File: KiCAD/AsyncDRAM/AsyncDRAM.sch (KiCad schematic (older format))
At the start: 6 parts

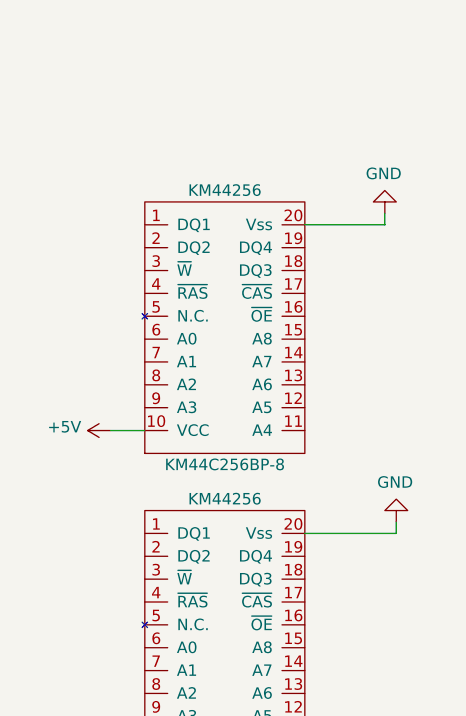
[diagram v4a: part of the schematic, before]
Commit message: Added ATmega809 Symbol
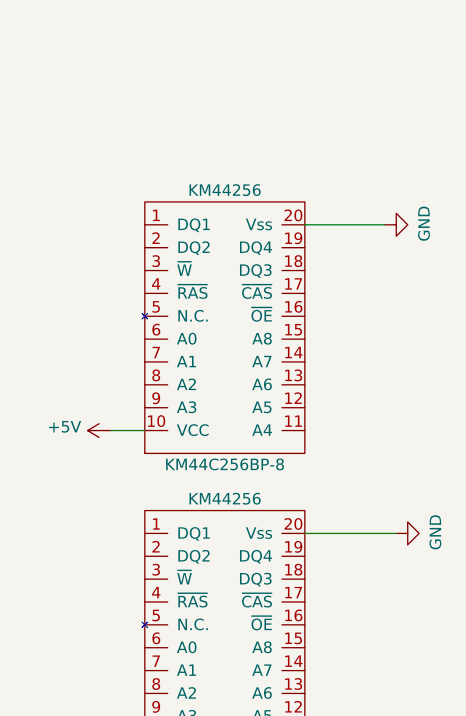
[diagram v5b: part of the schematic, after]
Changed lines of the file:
@@
 L Power:GND #PWR?
 U 1 1 5DAAFE76
-P 5300 1500
-F 0 "#PWR?" H 5300 1250 50  0001 C CNN
-F 1 "GND" H 5305 1327 50  0000 C CNN
-F 2 "" H 5300 1500 50  0001 C CNN
-F 3 "" H 5300 1500 50  0001 C CNN
-	1    5300 1500
-	-1   0    0    1
+P 5300 1550
+F 0 "#PWR?" H 5300 1300 50  0001 C CNN
+F 1 "GND" H 5305 1377 50  0000 C CNN
+F 2 "" H 5300 1550 50  0001 C CNN
+F 3 "" H 5300 1550 50  0001 C CNN
+	1    5300 1550
+	0    -1   -1   0
 $EndComp
 Wire Wire Line
 	4950 1550 5300 1550
-Wire Wire Line
-	5300 1550 5300 1500
 $Comp
 L Power:+5V #PWR?
@@
 L Power:GND #PWR?
 U 1 1 5DAB36DC
-P 5350 2850
-F 0 "#PWR?" H 5350 2600 50  0001 C CNN
-F 1 "GND" H 5355 2677 50  0000 C CNN
-F 2 "" H 5350 2850 50  0001 C CNN
-F 3 "" H 5350 2850 50  0001 C CNN
-	1    5350 2850
-	-1   0    0    1
+P 5350 2900
+F 0 "#PWR?" H 5350 2650 50  0001 C CNN
+F 1 "GND" H 5355 2727 50  0000 C CNN
+F 2 "" H 5350 2900 50  0001 C CNN
+F 3 "" H 5350 2900 50  0001 C CNN
+	1    5350 2900
+	0    -1   -1   0
 $EndComp
 Wire Wire Line
 	4950 2900 5350 2900
-Wire Wire Line
-	5350 2900 5350 2850
 $EndSCHEMATC

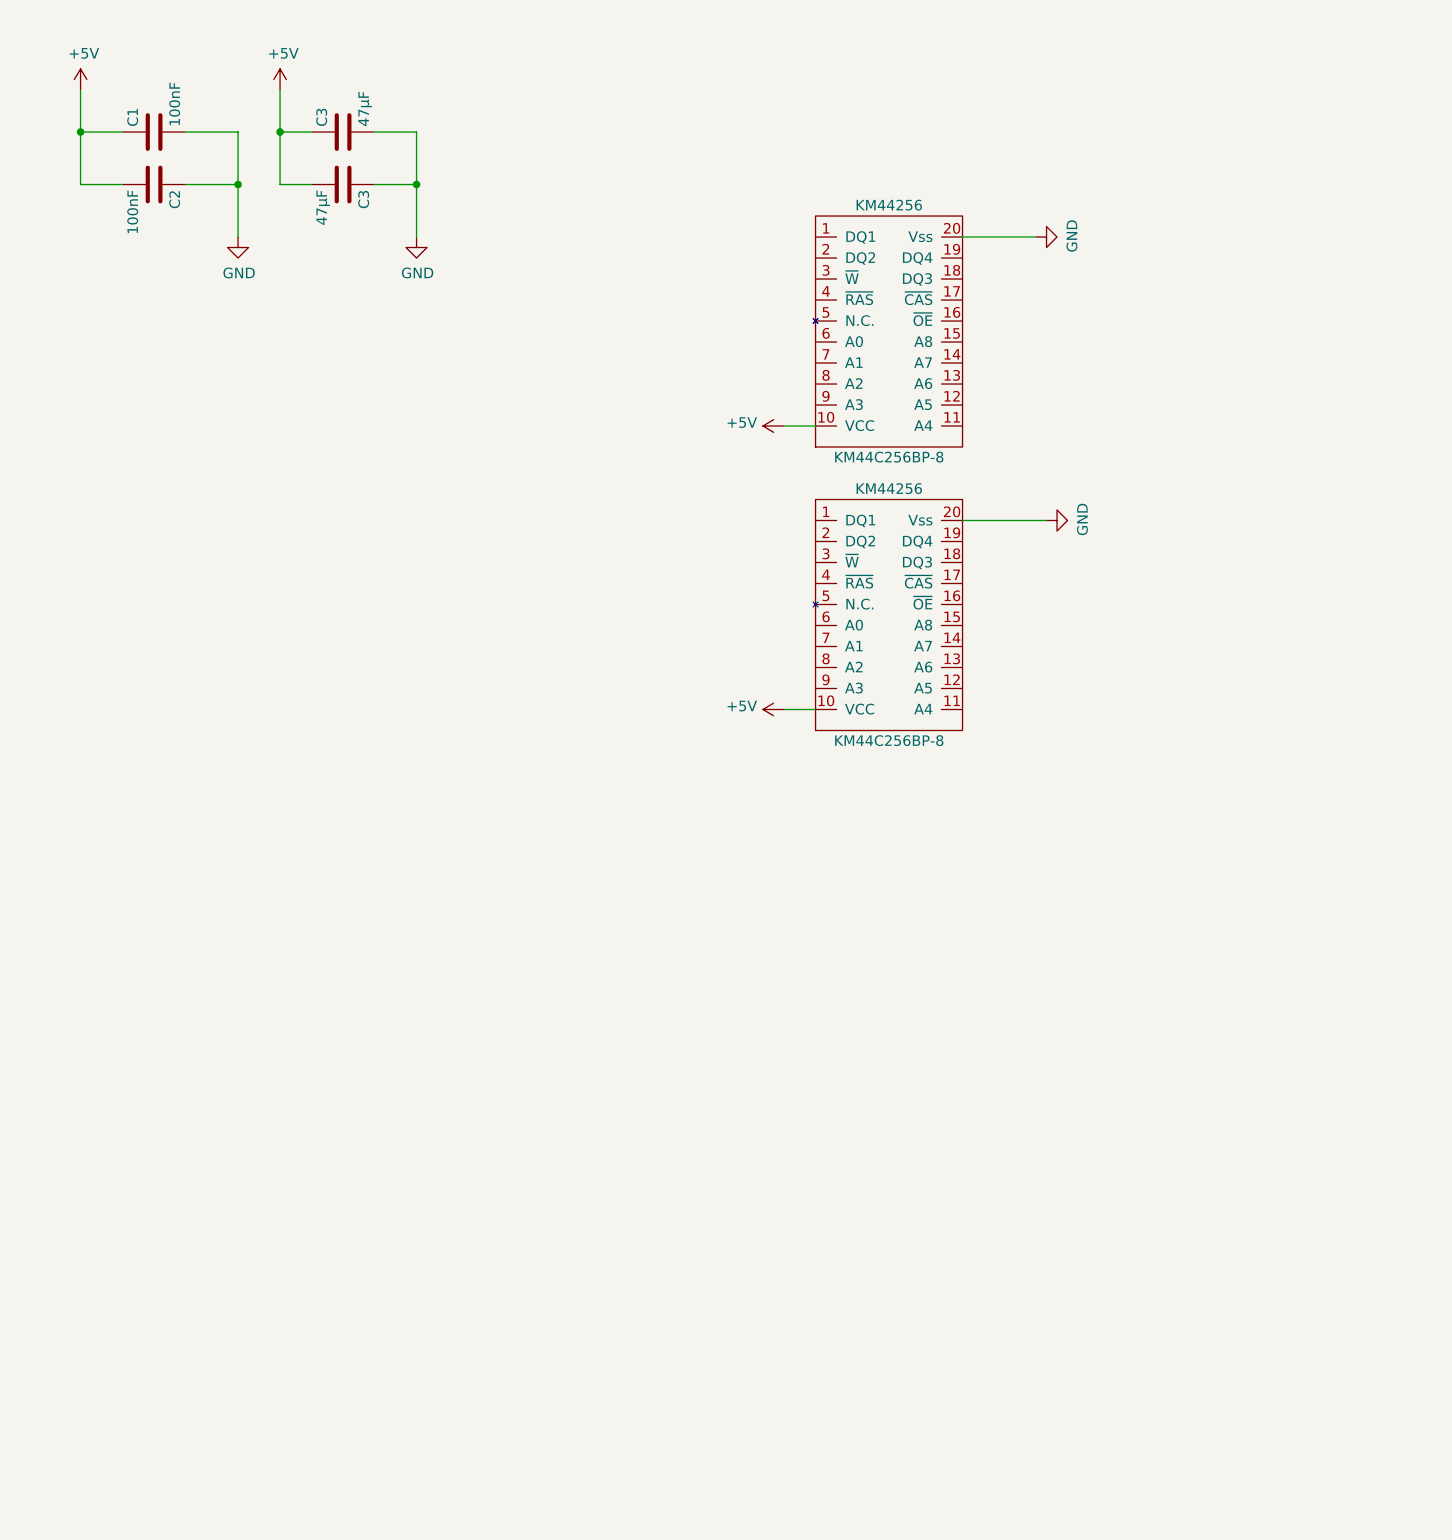
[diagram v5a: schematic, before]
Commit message: Added Reference Manual, Advanced schematic design
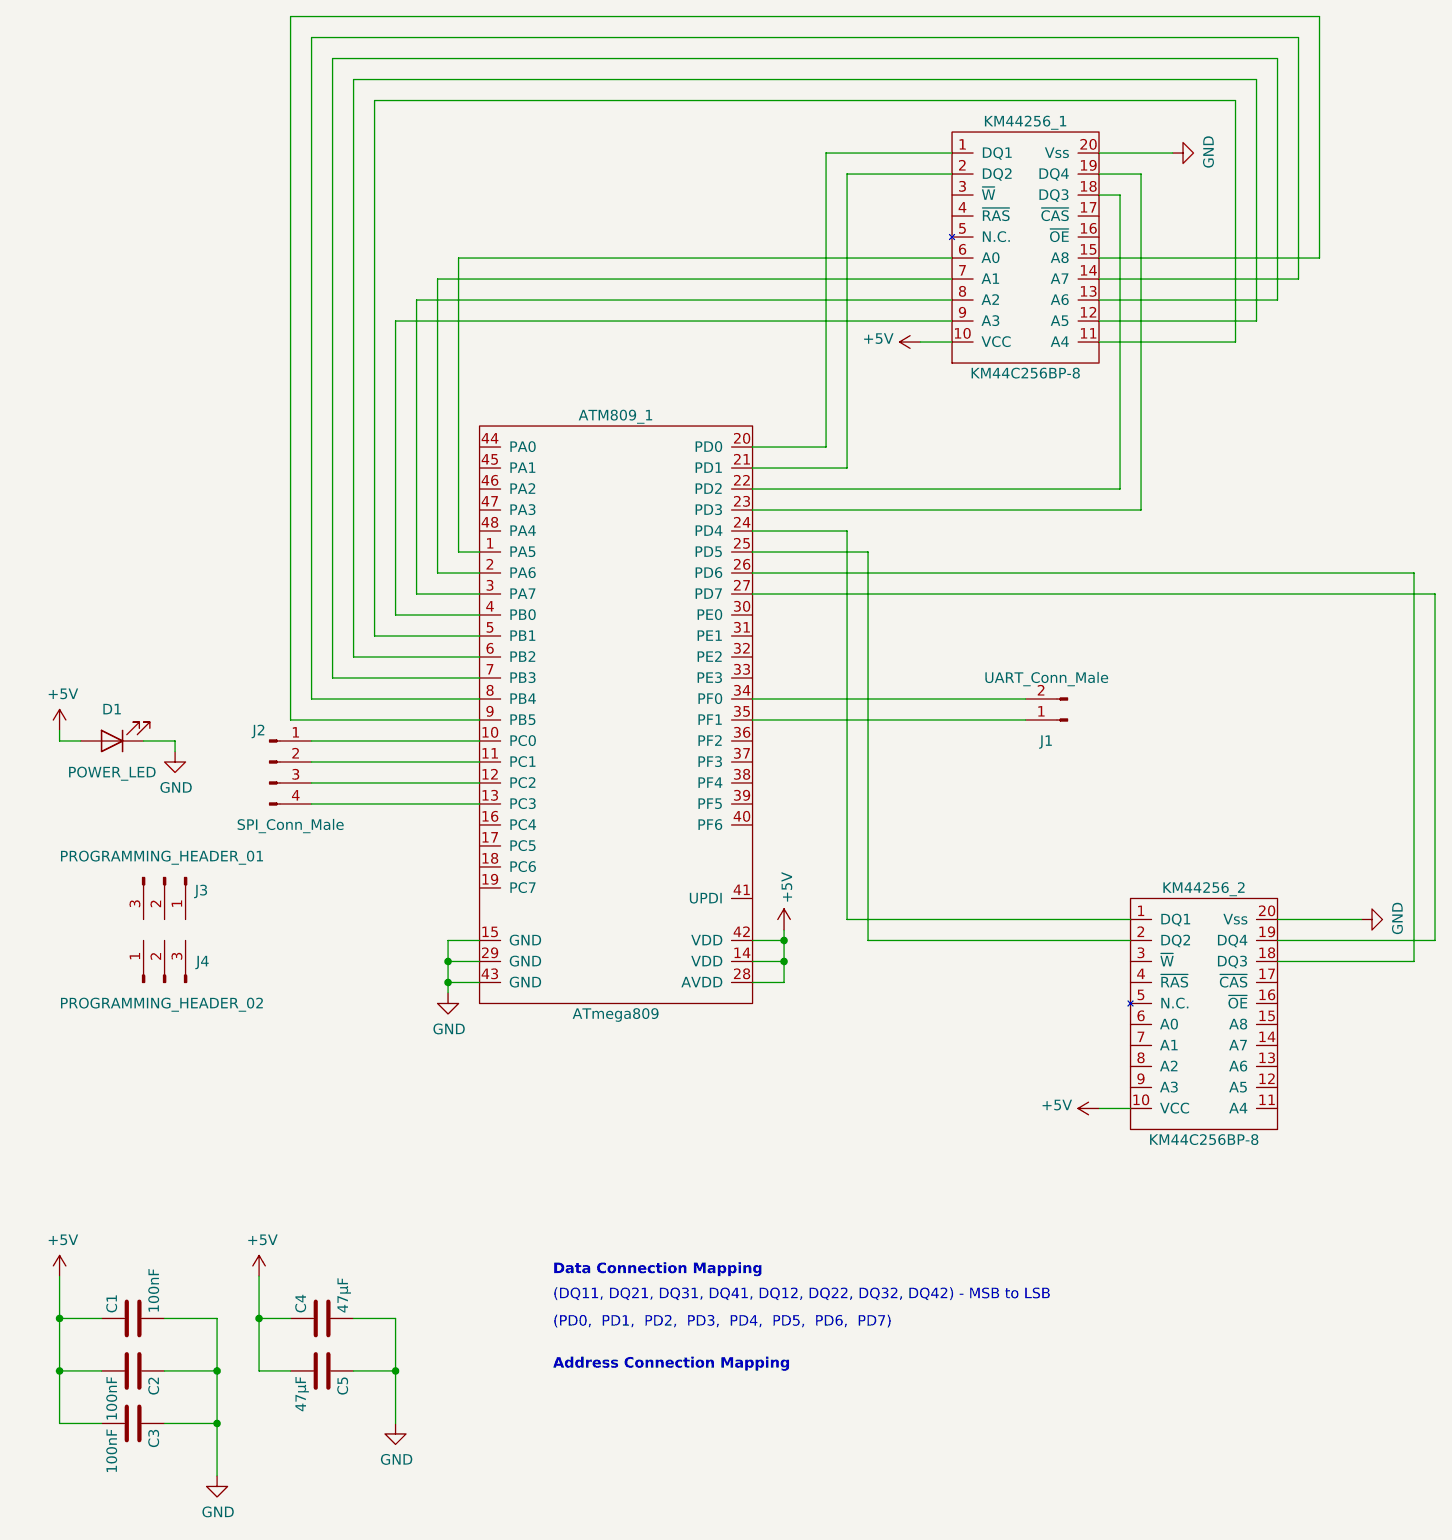
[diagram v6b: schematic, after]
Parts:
- added ATM809_1: ATmega809, symbol MyLibrary:ATmega809
- added C3: 100nF, symbol Device:C
- added D1: POWER_LED, symbol Device:LED
- added J1: UART_Conn_Male, symbol Connectors:Conn_01x02_Male
- added J2: SPI_Conn_Male, symbol Connectors:Conn_01x04_Male
- added J3: PROGRAMMING_HEADER_01, symbol Connectors:Conn_01x03_Male
- added J4: PROGRAMMING_HEADER_02, symbol Connectors:Conn_01x03_Male
- renumbered C3 to C4, C3 to C5, KM44256 to KM44256_1, KM44256 to KM44256_2
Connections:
- net +5V: now also ATM809_1.14 (VDD), ATM809_1.28 (AVDD), ATM809_1.42 (VDD), C3.2, D1.2 (A)
- net GND: now also ATM809_1.15 (GND), ATM809_1.29 (GND), ATM809_1.43 (GND), C3.1, D1.1 (K)
- net at KM44256_1.1 (DQ1): now also ATM809_1.20 (PD0)
- net at KM44256_1.11 (A4): now also ATM809_1.5 (PB1)
- net at KM44256_1.12 (A5): now also ATM809_1.6 (PB2)
- net at KM44256_1.13 (A6): now also ATM809_1.7 (PB3)
- net at KM44256_1.14 (A7): now also ATM809_1.8 (PB4)
- net at KM44256_1.15 (A8): now also ATM809_1.9 (PB5)
- net at KM44256_1.18 (DQ3): now also ATM809_1.22 (PD2)
- net at KM44256_1.19 (DQ4): now also ATM809_1.23 (PD3)
- net at KM44256_1.2 (DQ2): now also ATM809_1.21 (PD1)
- net at KM44256_1.6 (A0): now also ATM809_1.1 (PA5)
- net at KM44256_1.7 (A1): now also ATM809_1.2 (PA6)
- net at KM44256_1.8 (A2): now also ATM809_1.3 (PA7)
- net at KM44256_1.9 (A3): now also ATM809_1.4 (PB0)
- net at KM44256_2.1 (DQ1): now also ATM809_1.24 (PD4)
- net at KM44256_2.18 (DQ3): now also ATM809_1.26 (PD6)
- net at KM44256_2.19 (DQ4): now also ATM809_1.27 (PD7)
- net at KM44256_2.2 (DQ2): now also ATM809_1.25 (PD5)
- new net: ATM809_1.10 (PC0), J2.1 (Pin_1)
- new net: ATM809_1.11 (PC1), J2.2 (Pin_2)
- new net: ATM809_1.12 (PC2), J2.3 (Pin_3)
- new net: ATM809_1.13 (PC3), J2.4 (Pin_4)
- new net: ATM809_1.34 (PF0), J1.2 (Pin_2)
- new net: ATM809_1.35 (PF1), J1.1 (Pin_1)
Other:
- note added: "(DQ11, DQ21, DQ31, DQ41, DQ12, DQ22, DQ32, DQ42) - MSB to LSB\n\n"
- note added: "(PD0, PD1, PD2, PD3, PD4, PD5, PD6, PD7)"
- note added: "Address Connection Mapping"
- note added: "Data Connection Mapping"
- moved on the sheet: C1, C2, C4, C5, KM44256_1, KM44256_2

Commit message: Advanced Schematic
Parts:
- removed J1: UART_Conn_Male, symbol Connectors:Conn_01x02_Male
- removed J2: SPI_Conn_Male, symbol Connectors:Conn_01x04_Male
- removed J3: PROGRAMMING_HEADER_01, symbol Connectors:Conn_01x03_Male
- removed J4: PROGRAMMING_HEADER_02, symbol Connectors:Conn_01x03_Male
- added J1: UART, symbol Connectors_Generic:Conn_01x02
- added J2: SPI, symbol Connectors_Generic:Conn_01x04
- added J3: UPDI, symbol Connectors_Generic:Conn_02x03_Odd_Even
- added J4: POWER, symbol Connectors_Generic:Conn_01x02
- added R1: 470Ohm, symbol Device:R
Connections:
- net +5V: now also J3.2 (Pin_2), J4.2 (Pin_2), R1.2; no longer D1.2 (A)
- net GND: now also J3.6 (Pin_6), J4.1 (Pin_1)
- net D0: now reaches ATM809_1.20 (PD0), KM44256_1.1 (DQ1)
- net at ATM809_1.5 (PB1), KM44256_1.11 (A4): now also KM44256_2.11 (A4)
- net at ATM809_1.6 (PB2), KM44256_1.12 (A5): now also KM44256_2.12 (A5)
- net at ATM809_1.7 (PB3), KM44256_1.13 (A6): now also KM44256_2.13 (A6)
- net at ATM809_1.8 (PB4), KM44256_1.14 (A7): now also KM44256_2.14 (A7)
- net at ATM809_1.9 (PB5), KM44256_1.15 (A8): now also KM44256_2.15 (A8)
- net D2: now reaches ATM809_1.22 (PD2), KM44256_1.18 (DQ3)
- net D3: now reaches ATM809_1.23 (PD3), KM44256_1.19 (DQ4)
- net D1: now reaches ATM809_1.21 (PD1), KM44256_1.2 (DQ2)
- net at ATM809_1.1 (PA5), KM44256_1.6 (A0): now also KM44256_2.6 (A0)
- net at ATM809_1.2 (PA6), KM44256_1.7 (A1): now also KM44256_2.7 (A1)
- net at ATM809_1.3 (PA7), KM44256_1.8 (A2): now also KM44256_2.8 (A2)
- net at ATM809_1.4 (PB0), KM44256_1.9 (A3): now also KM44256_2.9 (A3)
- net D4: now reaches ATM809_1.24 (PD4), KM44256_2.1 (DQ1)
- net D6: now reaches ATM809_1.26 (PD6), KM44256_2.18 (DQ3)
- net D7: now reaches ATM809_1.27 (PD7), KM44256_2.19 (DQ4)
- net D5: now reaches ATM809_1.25 (PD5), KM44256_2.2 (DQ2)
- net at ATM809_1.10 (PC0): now also J2.4 (Pin_4)
- net at ATM809_1.11 (PC1): now also J2.3 (Pin_3)
- net at ATM809_1.12 (PC2): now also J2.2 (Pin_2)
- net at ATM809_1.13 (PC3): now also J2.1 (Pin_1)
- net at ATM809_1.34 (PF0): now also J1.1 (Pin_1)
- net at ATM809_1.35 (PF1): now also J1.2 (Pin_2)
- net at ATM809_1.41 (UPDI): now also J3.1 (Pin_1)
- new net: D1.2 (A), R1.1
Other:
- note added: "(A0, A1, A2, A3, A4, A5, A6, A7, A8, A9)"
- note added: "(PA5, PA6, PA7, PB0, PB1, PB2, PB3, PB4, PB5)"
- moved on the sheet: D1, KM44256_2
